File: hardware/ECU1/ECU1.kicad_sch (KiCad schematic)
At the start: 15 parts, among them J1 Micro_SD_Card, U1 step-down (buck), U2 MPU-6050, U3 ESP32-WROOM-32

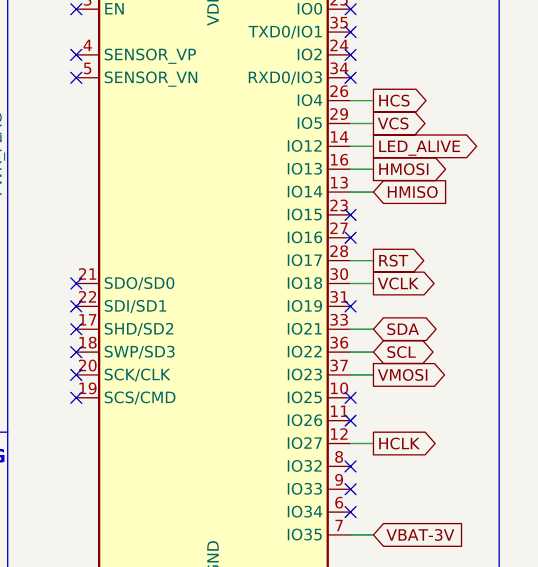
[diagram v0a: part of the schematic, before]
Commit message: fix label names
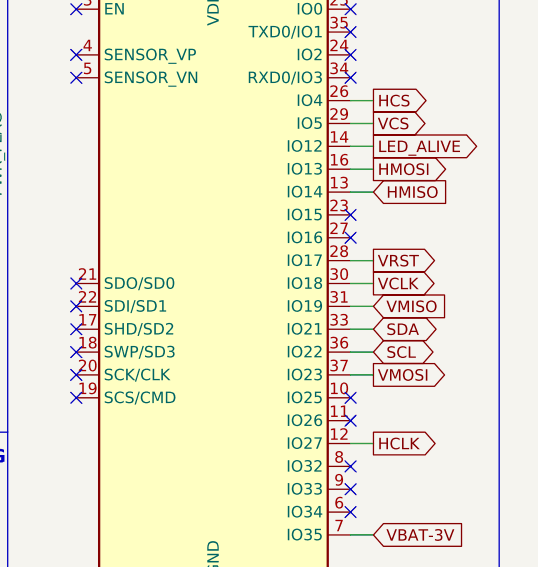
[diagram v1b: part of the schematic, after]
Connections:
- net RST: no longer U3.28 (IO17)
- net VMISO: now reaches U3.31 (IO19)
- new net VRST: U3.28 (IO17)
- no-connect marks 44 -> 43
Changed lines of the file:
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@@
   (title_block
     (title "ECU1")
-    (date "2022-09-23")
-    (rev "v2.0.5")
+    (date "2022-11-01")
+    (rev "v2.0.6")
     (company "Parahybaja")
     (comment 1 "demo version (only pinout)")
+    (comment 2 "fix VSPI pin's lable")
   )
   (junction (at 177.8 139.7) (diameter 0) (color 0 0 0 0)
@@
   (no_connect (at 168.91 88.9))
   (no_connect (at 168.91 93.98))
-  (no_connect (at 243.84 102.87))
   (no_connect (at 194.31 68.58))
   (no_connect (at 213.36 77.47))
@@
     (stroke (width 0) (type default) (color 0 0 0 0))
   )
+  (wire (pts (xy 243.84 102.87) (xy 246.38 102.87))
+    (stroke (width 0) (type default) (color 0 0 0 0))
+  )
   (wire (pts (xy 83.82 129.54) (xy 81.28 129.54))
     (stroke (width 0) (type default) (color 0 0 0 0))
@@
     )
   )
+  (global_label "VMISO" (shape input) (at 246.38 102.87 0) (fields_autoplaced)
+    (effects (font (size 1.27 1.27)) (justify left))
+    (property "Intersheet References" "${INTERSHEET_REFS}" (id 0) (at 254.4779 102.7906 0)
+      (effects (font (size 1.27 1.27)) (justify left) hide)
+    )
+  )
   (global_label "HMOSI" (shape output) (at 246.38 87.63 0) (fields_autoplaced)
     (effects (font (size 1.27 1.27)) (justify left))
@@
     )
   )
-  (global_label "RST" (shape output) (at 246.38 97.79 0) (fields_autoplaced)
-    (effects (font (size 1.27 1.27)) (justify left))
-    (property "Intersheet References" "${INTERSHEET_REFS}" (id 0) (at 252.2402 97.7106 0)
-      (effects (font (size 1.27 1.27)) (justify left) hide)
-    )
+  (global_label "VRST" (shape output) (at 246.38 97.79 0) (fields_autoplaced)
+    (effects (font (size 1.27 1.27)) (justify left))
+    (property "Intersheet References" "${INTERSHEET_REFS}" (id 0) (at 253.3288 97.7106 0)
+      (effects (font (size 1.27 1.27)) (justify left) hide)
+    )
